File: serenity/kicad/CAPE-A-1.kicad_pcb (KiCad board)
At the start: 4 copper layers, 55 x 35 mm, 25 parts, among them J1 PB2I-P1-2x18, J10 Nano-Fit-4P-POWER, J2 PB2I-P2-2x18, J3 JST-GH-4P-CAN, J4 JST-GH-4P-RS485, J5 JST-GH-4P-1553, J6 JST-GH-6P-ETH1, J7 JST-GH-6P-ETH2, J8 JST-GH-3P-ESC-TELEM, J9 1x8-SERVO-PWM, T1 SM-1553-11, U1 ICM-42688-P, U10 SLB9670, U2 BMP388, U3 SAM-M10Q-00B, U4 ATA6561, U5 MAX3485E, U6 DS26LV31, U7 DS26LV32, U8 DP83825I, U9 DP83825I

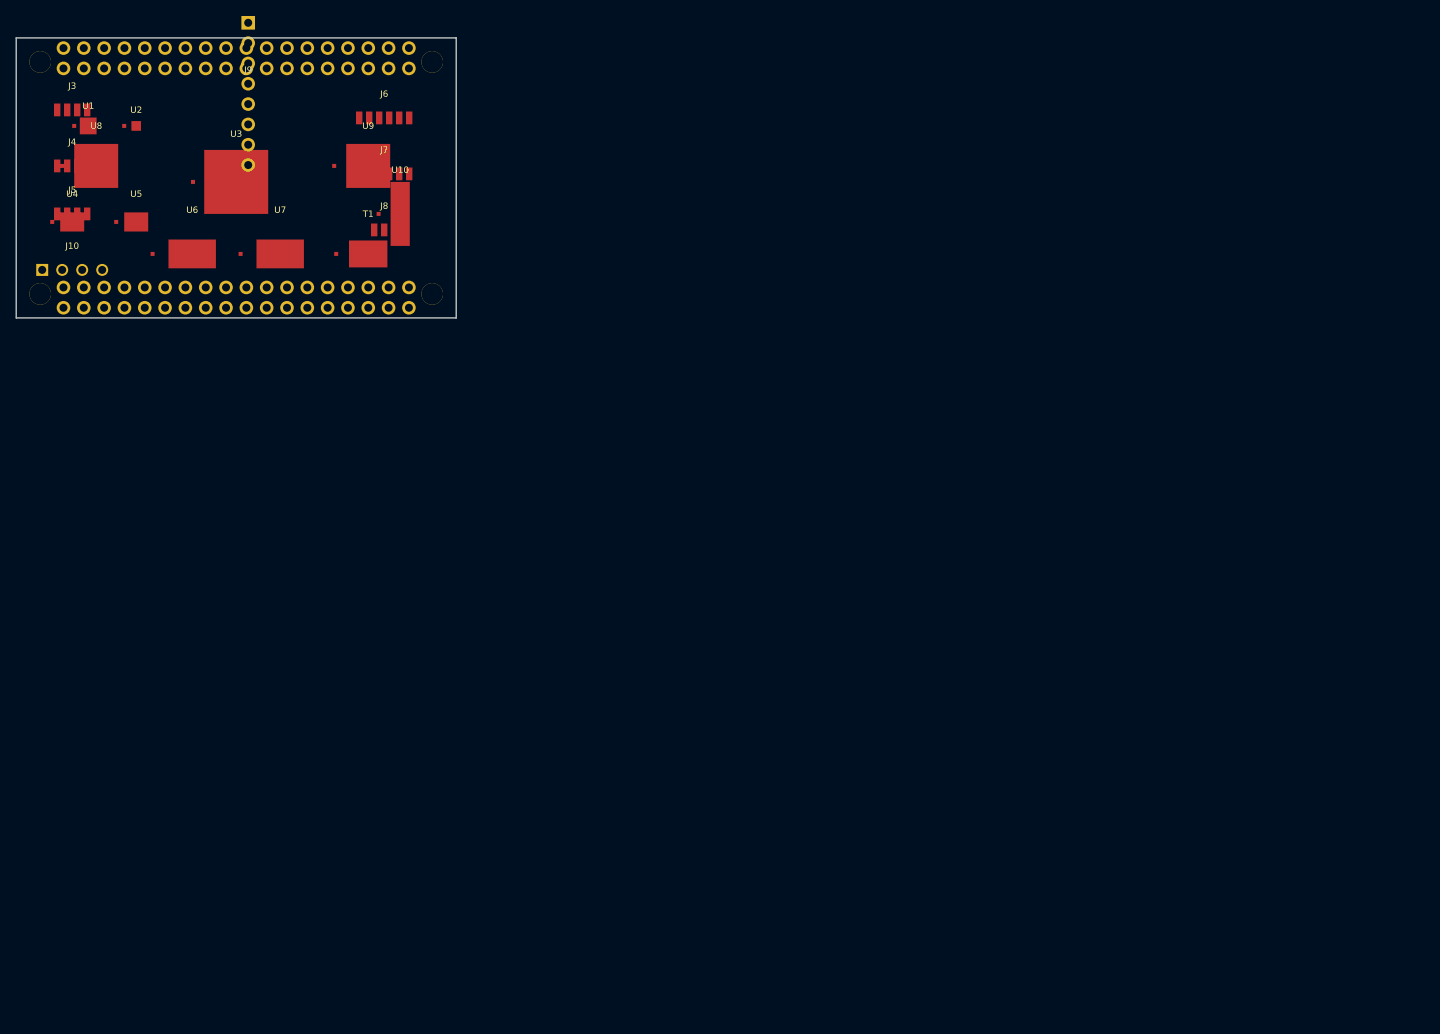
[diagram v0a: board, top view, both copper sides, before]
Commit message: Rev M: populate CAPE-A/B schematics and center PCBs on A4 drawing page
- CAPE-A-1.kicad_sch: full schematic with Conn_36 J1/J2 expansion headers
  (36 pins each, all nets labeled), ICM-42688-P, BMP388, SAM-M10Q, ATA6561,
  MAX3485E, DS26LV31/32, SM-1553-11, DP83825I×2, SLB9670; 142 global labels
  connecting expansion header nets to IC pins
- CAPE-B-1.kicad_sch: full schematic with RFM95W, WL1837MOD, ATA6561,
  MAX3485E, DS26LV31/32, SM-1553-11, DP83825I×2, SLB9670, ATF16V8BQL,
  W25Q128JV, DRV8833, HX711, PCA9685, microSD; 169 global labels
- CAPE-A-1.kicad_pcb, CAPE-B-1.kicad_pcb: board outline shifted from
  origin (0,0)–(55,35) to (121,87.5)–(176,122.5), centering 55×35mm board
  on A4 (297×210mm) drawing sheet; footprint absolute positions updated,
  inner relative pad/courtyard coordinates unchanged

Co-Authored-By: Claude Sonnet 4.6 <noreply@anthropic.com>
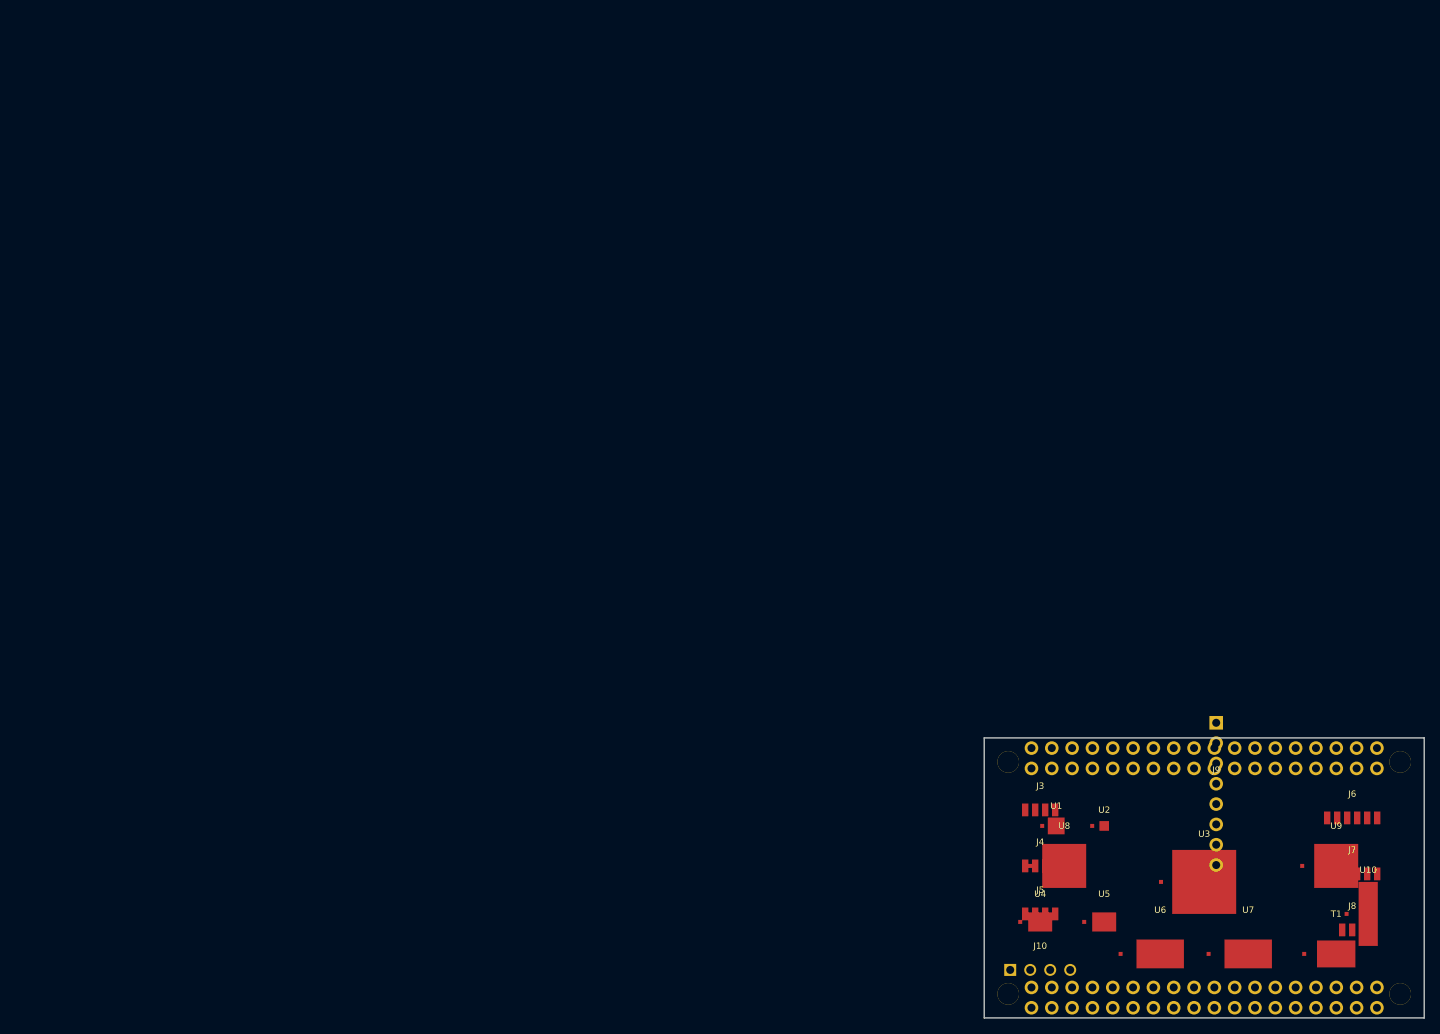
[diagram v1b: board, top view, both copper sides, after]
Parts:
- removed the ? at (3.00, 3.00)
- removed the ? at (52.0, 3.00)
- removed the ? at (3.00, 32.0)
- removed the ? at (52.0, 32.0)
- added ?: , MountingHole:MountingHole_2.7mm_M2.5, F.Cu at (124.0, 90.5)
- added ?: , MountingHole:MountingHole_2.7mm_M2.5, F.Cu at (173.0, 90.5)
- added ?: , MountingHole:MountingHole_2.7mm_M2.5, F.Cu at (124.0, 119.5)
- added ?: , MountingHole:MountingHole_2.7mm_M2.5, F.Cu at (173.0, 119.5)
- moved J1 149.3 mm to (148.5, 90.0)
- moved J10 149.3 mm to (128.0, 116.5)
- moved J2 149.3 mm to (148.5, 120.0)
- moved J3 149.3 mm to (128.0, 96.5)
- moved J4 149.3 mm to (128.0, 103.5)
- moved J5 149.3 mm to (128.0, 109.5)
- moved J6 149.3 mm to (167.0, 97.5)
- moved J7 149.3 mm to (167.0, 104.5)
- moved J8 149.3 mm to (167.0, 111.5)
- moved J9 149.3 mm to (150.0, 94.5)
- moved T1 149.3 mm to (165.0, 114.5)
- moved U1 149.3 mm to (130.0, 98.5)
- moved U10 149.3 mm to (169.0, 109.5)
- moved U2 149.3 mm to (136.0, 98.5)
- moved U3 149.3 mm to (148.5, 105.5)
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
